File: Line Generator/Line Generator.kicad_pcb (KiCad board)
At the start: 2 copper layers, 38.5 x 32.2 mm, 26 parts, among them J1 Conn_01x04, Q1 BS170F, Q2 BCV46, Q3 BCV46, Q4 BS170F

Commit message: PCB Layout altered for Adrian's Circuit design
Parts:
- R6: value 100K -> 4K7
- R7: value 4K7 -> 100K
- moved Q1 19.2 mm to (213.0, 88.5), turned to 180 degrees
- moved R3 18.0 mm to (209.2, 88.0), turned to 90 degrees
- moved RV1 13.0 mm to (236.8, 70.5), turned to 0 degrees
- moved RV2 13.0 mm to (236.8, 96.8), turned to 0 degrees
- moved R2 11.1 mm to (207.0, 71.8), turned to 0 degrees
- moved R4 10.9 mm to (205.0, 86.2), turned to 180 degrees
- moved R1 10.8 mm to (213.5, 84.8), turned to 180 degrees
- moved R5 9.75 mm to (205.0, 89.2), turned to 180 degrees
- moved JP2 9.37 mm to (227.2, 96.8), turned to 0 degrees
- moved R7 9.00 mm to (205.0, 91.8), turned to 0 degrees
- moved C2 8.98 mm to (205.0, 97.5), turned to 180 degrees
- moved Q4 8.75 mm to (212.8, 94.2), turned to 180 degrees
- moved R6 7.50 mm to (209.5, 94.8)
- moved R8 7.35 mm to (211.5, 98.2)
- moved Q2 7.32 mm to (217.0, 88.2)
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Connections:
- C1 pad 2: Net-(C1-Pad2) -> +12V
- C2 pad 2: Net-(C2-Pad2) -> +12V
- D1 pad 2: Net-(C1-Pad1) -> Net-(D1-Pad2)
- D3 pad 2: Net-(C2-Pad1) -> Net-(D3-Pad2)
- JP1 pad 1: +12V -> Net-(D1-Pad2)
- JP1 pad 2: Net-(C1-Pad2) -> Net-(C1-Pad1)
- JP2 pad 1: +12V -> Net-(D3-Pad2)
- JP2 pad 2: Net-(C2-Pad2) -> Net-(C2-Pad1)
- R2 pad 2: Net-(C1-Pad1) -> Net-(D1-Pad2)
- R3 pad 1: Net-(C1-Pad1) -> Net-(D1-Pad2)
- R4 pad 1: +12V -> Net-(Q2-Pad2)
- R4 pad 2: Net-(Q2-Pad2) -> +12V
- R6 pad 1: +12V -> Net-(D3-Pad2)
- R6 pad 2: Net-(C2-Pad1) -> Net-(Q4-Pad3)
- R7 pad 1: Net-(C2-Pad1) -> +12V
- R7 pad 2: Net-(Q4-Pad3) -> Net-(D3-Pad2)
- R8 pad 1: Laser1 -> Net-(Q4-Pad1)
- R8 pad 2: Net-(Q4-Pad1) -> Laser1
- RV1 pad 1: Net-(C1-Pad2) -> +12V
- RV1 pad 3: Net-(RV1-Pad3) -> Net-(D1-Pad2)
- RV2 pad 1: Net-(C2-Pad2) -> +12V
- RV2 pad 3: Net-(RV2-Pad3) -> Net-(D3-Pad2)
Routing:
- net Net-(D1-Pad2): track 0.00 -> 37.2 mm
- net Net-(D3-Pad2): track 0.00 -> 29.1 mm
- net Laser1: track 11.9 -> 30.6 mm
- net Laser2: track 22.0 -> 4.84 mm
- net GND: track 62.0 -> 48.8 mm
- net Net-(Q2-Pad2): track 2.48 -> 13.5 mm
- net Net-(C1-Pad2): track 10.8 -> 0.00 mm
- net Net-(C2-Pad2): track 9.33 -> 0.00 mm
- net +12V: track 104.7 -> 95.4 mm
- net Net-(Q3-Pad2): track 3.63 -> 12.3 mm
- net Net-(C1-Pad1): track 37.7 -> 45.0 mm
- net Net-(D2-Pad3): track 12.9 -> 18.1 mm
- net Net-(C2-Pad1): track 42.2 -> 40.6 mm
- net Net-(D2-Pad1): track 12.7 -> 14.2 mm
- net Net-(Q1-Pad1): track 6.79 -> 5.67 mm
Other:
- board text added: "Only bridge jumper if pot not in place"

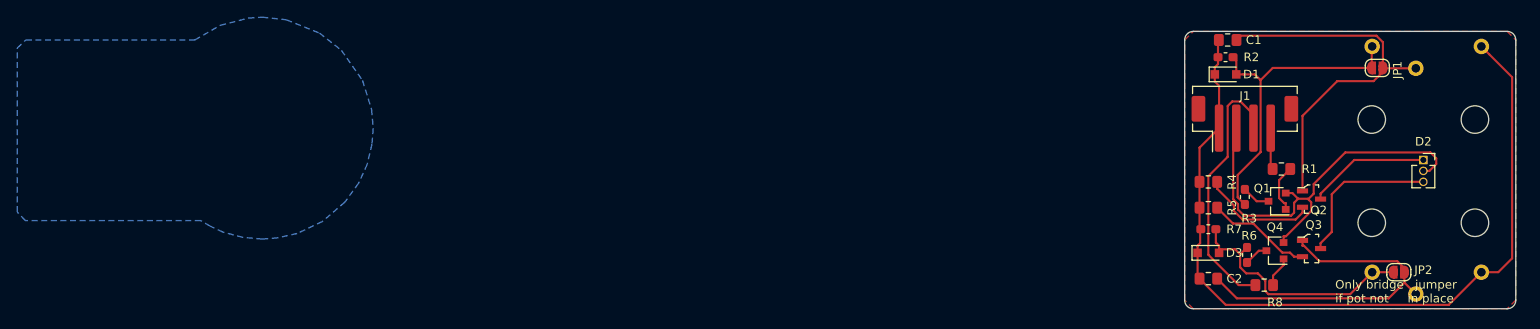
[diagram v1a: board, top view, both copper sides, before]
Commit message: Track widths increased
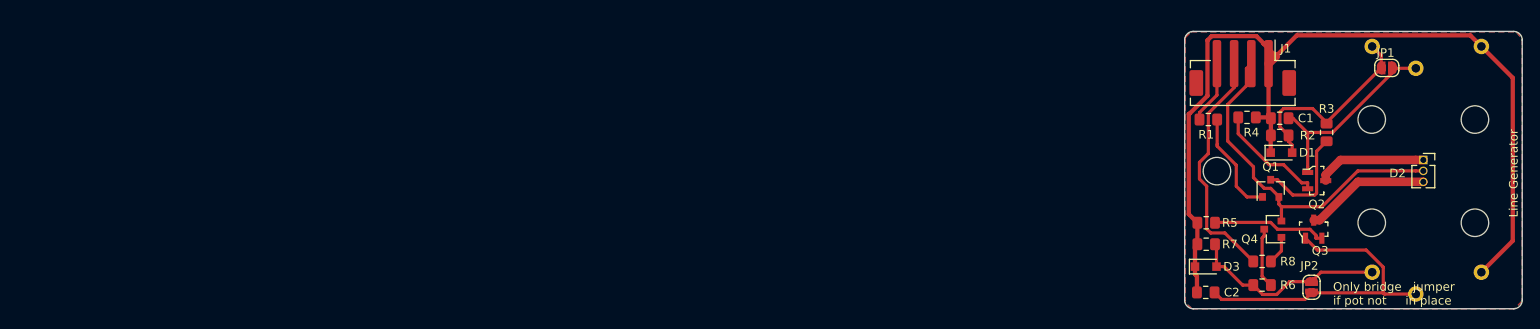
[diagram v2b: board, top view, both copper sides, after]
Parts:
- added Mount5: MountingHole_3.2mm_M3_ISO7380, MountingHole:MountingHole_3.2mm_M3_ISO7380, F.Cu at (206.0, 85.0)
- R2, R3, R6, R7: footprint Resistor_SMD:R_0603_1608Metric_Pad1.05x0.95mm_HandSolder -> Resistor_SMD:R_0805_2012Metric_Pad1.15x1.40mm_HandSolder
- moved R3 12.1 mm to (218.8, 80.5), turned to 270 degrees
- moved D1 11.2 mm to (213.5, 82.8)
- moved R2 11.1 mm to (213.3, 80.8)
- moved C1 10.9 mm to (213.3, 78.8)
- moved JP2 10.3 mm to (217.0, 98.5), turned to 270 degrees
- moved R1 10.3 mm to (205.0, 79.0)
- moved R4 8.75 mm to (209.5, 78.8), turned to 0 degrees
- moved J1 6.50 mm to (209.0, 73.0), turned to 180 degrees
- moved R6 3.91 mm to (211.2, 98.2), turned to 0 degrees
- moved R8 2.76 mm to (211.2, 95.5)
- moved Q4 2.51 mm to (212.5, 91.8)
- moved Q3 2.26 mm to (217.2, 91.8), turned to 90 degrees
- moved Q2 2.23 mm to (217.6, 86.1)
- moved R5 1.77 mm to (204.8, 91.0)
- moved R7 1.77 mm to (204.8, 93.5)
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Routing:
- net Net-(C1-Pad1): track 45.0 -> 23.6 mm
- net +12V: track 95.4 -> 109.1 mm
- net Net-(D1-Pad2): track 37.2 -> 23.6 mm
- net Net-(Q1-Pad3): track 3.32 -> 12.7 mm
- net GND: track 48.8 -> 40.7 mm
- net Net-(Q1-Pad1): track 5.67 -> 12.2 mm
- net Net-(D3-Pad2): track 29.1 -> 23.2 mm
- net Net-(Q4-Pad3): track 2.82 -> 7.02 mm
- net Net-(D2-Pad3): track 18.1 -> 14.6 mm
- net Net-(C2-Pad1): track 40.6 -> 37.5 mm
- net Laser2: track 4.84 -> 7.34 mm
- net Laser1: track 30.6 -> 28.2 mm
- net Net-(D2-Pad1): track 14.2 -> 12.7 mm
- net Net-(Q3-Pad2): track 12.3 -> 13.4 mm
- net Net-(Q2-Pad2): track 13.5 -> 13.0 mm
- added copper zone on B.Cu, net GND
- removed copper zone on B.Cu, net (none)
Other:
- board size 38.5 x 32.2 mm -> 39.2 x 32.2 mm
- board text added: "Line Generator"
